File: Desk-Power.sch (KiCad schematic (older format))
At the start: 17 parts, among them J1 USB_A, J2 USB_A, J3 USB_A, J4 USB_A, J5 USB_A, J6 USB_A, J7 USB_A, J8 USB_A, J9 USB_A, U1 TPS5430DDA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

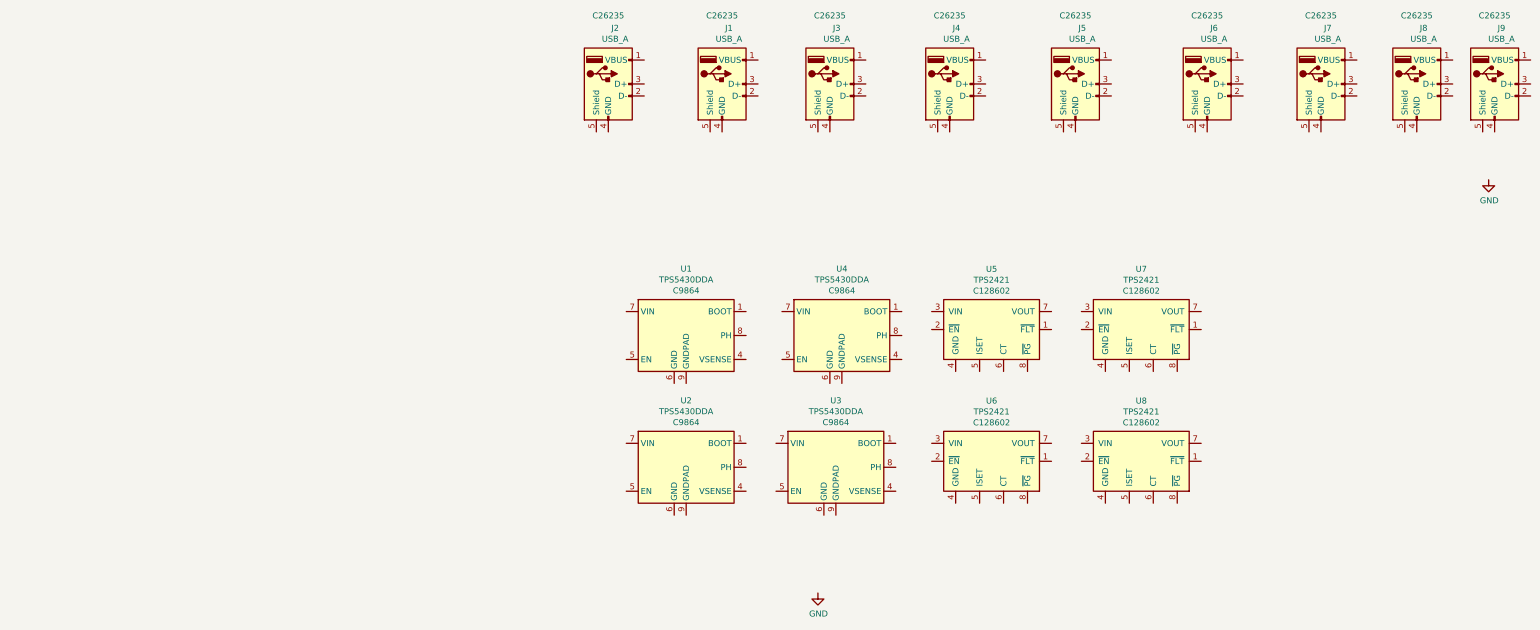
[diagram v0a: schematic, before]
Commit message: add new component packages
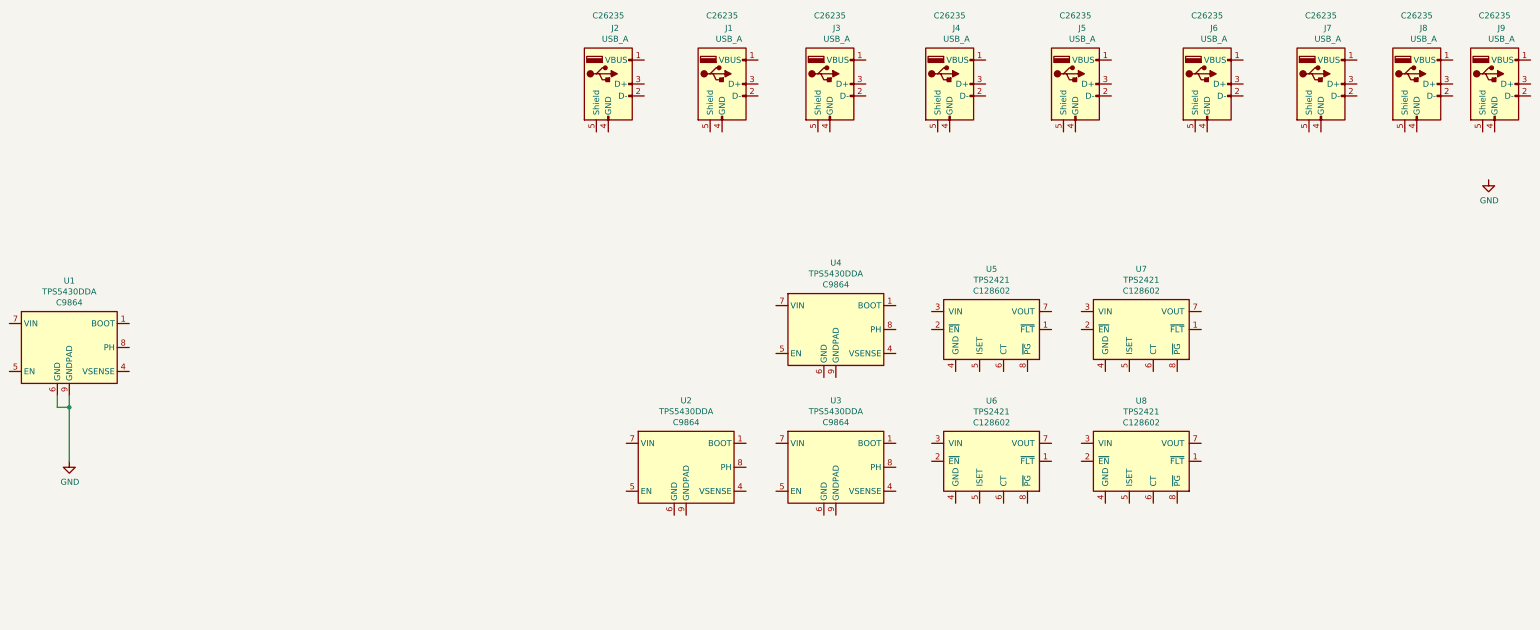
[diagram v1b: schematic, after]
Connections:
- net GND: now also U1.6 (GND), U1.9 (GNDPAD)
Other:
- moved on the sheet: U1, U4
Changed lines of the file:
@@
 L Regulator_Switching:TPS5430DDA U4
 U 1 1 602942E3
-P 9450 6250
-F 0 "U4" H 9450 6807 50  0000 C CNN
-F 1 "TPS5430DDA" H 9450 6716 50  0000 C CNN
-F 2 "Package_SO:TI_SO-PowerPAD-8_ThermalVias" H 9500 5900 50  0001 L CIN
-F 3 "http://www.ti.com/lit/ds/symlink/tps5430.pdf" H 9450 6250 50  0001 C CNN
-F 4 "C9864" H 9450 6625 50  0000 C CNN "LCSC #"
-	1    9450 6250
+P 9400 6200
+F 0 "U4" H 9400 6757 50  0000 C CNN
+F 1 "TPS5430DDA" H 9400 6666 50  0000 C CNN
+F 2 "Package_SO:TI_SO-PowerPAD-8_ThermalVias" H 9450 5850 50  0001 L CIN
+F 3 "http://www.ti.com/lit/ds/symlink/tps5430.pdf" H 9400 6200 50  0001 C CNN
+F 4 "C9864" H 9400 6575 50  0000 C CNN "LCSC #"
+	1    9400 6200
 	1    0    0    -1
 $EndComp
@@
 L Regulator_Switching:TPS5430DDA U1
 U 1 1 60296023
-P 8150 6250
-F 0 "U1" H 8150 6807 50  0000 C CNN
-F 1 "TPS5430DDA" H 8150 6716 50  0000 C CNN
-F 2 "Package_SO:TI_SO-PowerPAD-8_ThermalVias" H 8200 5900 50  0001 L CIN
-F 3 "http://www.ti.com/lit/ds/symlink/tps5430.pdf" H 8150 6250 50  0001 C CNN
-F 4 "C9864" H 8150 6625 50  0000 C CNN "LCSC #"
-	1    8150 6250
+P 3000 6350
+F 0 "U1" H 3000 6907 50  0000 C CNN
+F 1 "TPS5430DDA" H 3000 6816 50  0000 C CNN
+F 2 "Package_SO:TI_SO-PowerPAD-8_ThermalVias" H 3050 6000 50  0001 L CIN
+F 3 "http://www.ti.com/lit/ds/symlink/tps5430.pdf" H 3000 6350 50  0001 C CNN
+F 4 "C9864" H 3000 6725 50  0000 C CNN "LCSC #"
+	1    3000 6350
 	1    0    0    -1
 $EndComp
@@
 L power:GND #PWR0102
 U 1 1 602A193B
-P 9250 8400
-F 0 "#PWR0102" H 9250 8150 50  0001 C CNN
-F 1 "GND" H 9255 8227 50  0000 C CNN
-F 2 "" H 9250 8400 50  0001 C CNN
-F 3 "" H 9250 8400 50  0001 C CNN
-	1    9250 8400
+P 3000 7300
+F 0 "#PWR0102" H 3000 7050 50  0001 C CNN
+F 1 "GND" H 3005 7127 50  0000 C CNN
+F 2 "" H 3000 7300 50  0001 C CNN
+F 3 "" H 3000 7300 50  0001 C CNN
+	1    3000 7300
 	1    0    0    -1
 $EndComp
@@
 	1    0    0    -1
 $EndComp
+Wire Wire Line
+	3000 6750 3000 6850
+Wire Wire Line
+	2900 6750 2900 6850
+Wire Wire Line
+	2900 6850 3000 6850
+Connection ~ 3000 6850
+Wire Wire Line
+	3000 6850 3000 7300
 $EndSCHEMATC
